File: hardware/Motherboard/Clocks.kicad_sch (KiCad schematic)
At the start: 7 parts, among them U60 74LS04, U61 74LS193, Y1 14MHz

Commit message: WIP
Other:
- moved on the sheet: C1, C2, R20, R21, U60D, U60E, U60F, U61, Y1

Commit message: WIP -rom pack
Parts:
- renumbered C2 to C1, C1 to C2, R20 to R5, R21 to R6, U60 to U31, U61 to U60
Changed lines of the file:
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@@
 		)
 	)
-	(global_label "CLK_3.5MHz"
+	(hierarchical_label "CLK_7MHz"
 		(shape output)
-		(at 223.52 81.28 0)
-		(fields_autoplaced yes)
+		(at 223.52 78.74 0)
 		(effects
 			(font
@@
 			(justify left)
 		)
-		(property "Intersheetrefs" "${INTERSHEET_REFS}"
-			(at 237.8747 81.28 0)
-			(effects
-				(font
-					(size 1.27 1.27)
-				)
-				(justify left)
-				(hide yes)
-			)
-		)
-	)
-	(global_label "CLK_1.75MHz"
+	)
+	(hierarchical_label "CLK_14MHz"
 		(shape output)
-		(at 223.52 83.82 0)
-		(fields_autoplaced yes)
+		(at 223.52 124.46 0)
 		(effects
 			(font
@@
 			(justify left)
 		)
-		(property "Intersheetrefs" "${INTERSHEET_REFS}"
-			(at 239.0842 83.82 0)
-			(effects
-				(font
-					(size 1.27 1.27)
-				)
-				(justify left)
-				(hide yes)
-			)
-		)
-	)
-	(global_label "CLK_7MHz"
+	)
+	(hierarchical_label "CLK_1.75MHz"
 		(shape output)
-		(at 223.52 78.74 0)
-		(fields_autoplaced yes)
+		(at 223.52 83.82 0)
 		(effects
 			(font
@@
 			(justify left)
 		)
-		(property "Intersheetrefs" "${INTERSHEET_REFS}"
-			(at 236.0604 78.74 0)
-			(effects
-				(font
-					(size 1.27 1.27)
-				)
-				(justify left)
-				(hide yes)
-			)
-		)
-	)
-	(global_label "CLK_14MHz"
+	)
+	(hierarchical_label "CLK_3.5MHz"
 		(shape output)
-		(at 223.52 124.46 0)
-		(fields_autoplaced yes)
+		(at 223.52 81.28 0)
 		(effects
 			(font
@@
 			(justify left)
 		)
-		(property "Intersheetrefs" "${INTERSHEET_REFS}"
-			(at 237.2699 124.46 0)
-			(effects
-				(font
-					(size 1.27 1.27)
-				)
-				(justify left)
-				(hide yes)
-			)
-		)
 	)
 	(symbol
@@
 		(dnp no)
 		(fields_autoplaced yes)
-		(property "Reference" "R21"
+		(property "Reference" "R6"
 			(at 104.14 104.14 90)
 			(effects
@@
 		(instances
 			(project "Squale"
-				(path "/9e981419-a202-4dd8-b7ec-e1bde8e7b185/7c4c7ab9-cc93-441e-893a-6812d858b558"
-					(reference "R21")
+				(path "/9e981419-a202-4dd8-b7ec-e1bde8e7b185/70613a33-7fd7-4f8d-95ce-cdec7974bf7d"
+					(reference "R6")
 					(unit 1)
 				)
@@
 		(dnp no)
 		(fields_autoplaced yes)
-		(property "Reference" "R20"
+		(property "Reference" "R5"
 			(at 77.47 104.14 90)
 			(effects
@@
 		)
 		(instances
-			(project ""
-				(path "/9e981419-a202-4dd8-b7ec-e1bde8e7b185/7c4c7ab9-cc93-441e-893a-6812d858b558"
-					(reference "R20")
+			(project "Squale"
+				(path "/9e981419-a202-4dd8-b7ec-e1bde8e7b185/70613a33-7fd7-4f8d-95ce-cdec7974bf7d"
+					(reference "R5")
 					(unit 1)
 				)
@@
 		(dnp no)
 		(fields_autoplaced yes)
-		(property "Reference" "C2"
+		(property "Reference" "C1"
 			(at 91.44 88.9 90)
 			(effects
@@
 		)
 		(instances
-			(project ""
-				(path "/9e981419-a202-4dd8-b7ec-e1bde8e7b185/7c4c7ab9-cc93-441e-893a-6812d858b558"
-					(reference "C2")
+			(project "Squale"
+				(path "/9e981419-a202-4dd8-b7ec-e1bde8e7b185/70613a33-7fd7-4f8d-95ce-cdec7974bf7d"
+					(reference "C1")
 					(unit 1)
 				)
@@
 		(dnp no)
 		(fields_autoplaced yes)
-		(property "Reference" "U60"
+		(property "Reference" "U31"
 			(at 129.54 87.63 0)
 			(effects
@@
 		)
 		(instances
-			(project ""
-				(path "/9e981419-a202-4dd8-b7ec-e1bde8e7b185/7c4c7ab9-cc93-441e-893a-6812d858b558"
-					(reference "U60")
+			(project "Squale"
+				(path "/9e981419-a202-4dd8-b7ec-e1bde8e7b185/70613a33-7fd7-4f8d-95ce-cdec7974bf7d"
+					(reference "U31")
 					(unit 4)
 				)
@@
 		(dnp no)
 		(fields_autoplaced yes)
-		(property "Reference" "U61"
+		(property "Reference" "U60"
 			(at 183.7533 71.12 0)
 			(effects
@@
 		)
 		(instances
-			(project ""
-				(path "/9e981419-a202-4dd8-b7ec-e1bde8e7b185/7c4c7ab9-cc93-441e-893a-6812d858b558"
-					(reference "U61")
+			(project "Squale"
+				(path "/9e981419-a202-4dd8-b7ec-e1bde8e7b185/70613a33-7fd7-4f8d-95ce-cdec7974bf7d"
+					(reference "U60")
 					(unit 1)
 				)
@@
 		(instances
 			(project "Squale"
-				(path "/9e981419-a202-4dd8-b7ec-e1bde8e7b185/7c4c7ab9-cc93-441e-893a-6812d858b558"
+				(path "/9e981419-a202-4dd8-b7ec-e1bde8e7b185/70613a33-7fd7-4f8d-95ce-cdec7974bf7d"
 					(reference "Y1")
 					(unit 1)
@@
 		(dnp no)
 		(fields_autoplaced yes)
-		(property "Reference" "#PWR0171"
+		(property "Reference" "#PWR0168"
 			(at 172.72 91.44 0)
 			(effects
@@
 		(instances
 			(project "Squale"
-				(path "/9e981419-a202-4dd8-b7ec-e1bde8e7b185/7c4c7ab9-cc93-441e-893a-6812d858b558"
-					(reference "#PWR0171")
+				(path "/9e981419-a202-4dd8-b7ec-e1bde8e7b185/70613a33-7fd7-4f8d-95ce-cdec7974bf7d"
+					(reference "#PWR0168")
 					(unit 1)
 				)
@@
 		(dnp no)
 		(fields_autoplaced yes)
-		(property "Reference" "#PWR0170"
+		(property "Reference" "#PWR0169"
 			(at 172.72 99.06 0)
 			(effects
@@
 		(instances
 			(project "Squale"
-				(path "/9e981419-a202-4dd8-b7ec-e1bde8e7b185/7c4c7ab9-cc93-441e-893a-6812d858b558"
-					(reference "#PWR0170")
+				(path "/9e981419-a202-4dd8-b7ec-e1bde8e7b185/70613a33-7fd7-4f8d-95ce-cdec7974bf7d"
+					(reference "#PWR0169")
 					(unit 1)
 				)
@@
 		(dnp no)
 		(fields_autoplaced yes)
-		(property "Reference" "U60"
+		(property "Reference" "U31"
 			(at 105.41 87.63 0)
 			(effects
@@
 		)
 		(instances
-			(project ""
-				(path "/9e981419-a202-4dd8-b7ec-e1bde8e7b185/7c4c7ab9-cc93-441e-893a-6812d858b558"
-					(reference "U60")
+			(project "Squale"
+				(path "/9e981419-a202-4dd8-b7ec-e1bde8e7b185/70613a33-7fd7-4f8d-95ce-cdec7974bf7d"
+					(reference "U31")
 					(unit 5)
 				)
@@
 		(dnp no)
 		(fields_autoplaced yes)
-		(property "Reference" "#PWR0169"
+		(property "Reference" "#PWR0170"
 			(at 181.61 74.93 0)
 			(effects
@@
 		(instances
 			(project "Squale"
-				(path "/9e981419-a202-4dd8-b7ec-e1bde8e7b185/7c4c7ab9-cc93-441e-893a-6812d858b558"
-					(reference "#PWR0169")
+				(path "/9e981419-a202-4dd8-b7ec-e1bde8e7b185/70613a33-7fd7-4f8d-95ce-cdec7974bf7d"
+					(reference "#PWR0170")
 					(unit 1)
 				)
@@
 		(dnp no)
 		(fields_autoplaced yes)
-		(property "Reference" "U60"
+		(property "Reference" "U31"
 			(at 77.47 87.63 0)
 			(effects
@@
 		)
 		(instances
-			(project ""
-				(path "/9e981419-a202-4dd8-b7ec-e1bde8e7b185/7c4c7ab9-cc93-441e-893a-6812d858b558"
-					(reference "U60")
+			(project "Squale"
+				(path "/9e981419-a202-4dd8-b7ec-e1bde8e7b185/70613a33-7fd7-4f8d-95ce-cdec7974bf7d"
+					(reference "U31")
 					(unit 6)
 				)
@@
 		(dnp no)
 		(fields_autoplaced yes)
-		(property "Reference" "U60"
+		(property "Reference" "U31"
 			(at 161.29 148.59 0)
 			(effects
@@
 		)
 		(instances
-			(project ""
-				(path "/9e981419-a202-4dd8-b7ec-e1bde8e7b185/7c4c7ab9-cc93-441e-893a-6812d858b558"
-					(reference "U60")
+			(project "Squale"
+				(path "/9e981419-a202-4dd8-b7ec-e1bde8e7b185/70613a33-7fd7-4f8d-95ce-cdec7974bf7d"
+					(reference "U31")
 					(unit 1)
 				)
@@
 		(dnp no)
 		(fields_autoplaced yes)
-		(property "Reference" "U60"
+		(property "Reference" "U31"
 			(at 161.29 163.83 0)
 			(effects
@@
 		)
 		(instances
-			(project ""
-				(path "/9e981419-a202-4dd8-b7ec-e1bde8e7b185/7c4c7ab9-cc93-441e-893a-6812d858b558"
-					(reference "U60")
+			(project "Squale"
+				(path "/9e981419-a202-4dd8-b7ec-e1bde8e7b185/70613a33-7fd7-4f8d-95ce-cdec7974bf7d"
+					(reference "U31")
 					(unit 2)
 				)
@@
 		(dnp no)
 		(fields_autoplaced yes)
-		(property "Reference" "U60"
+		(property "Reference" "U31"
 			(at 161.29 180.34 0)
 			(effects
@@
 		)
 		(instances
-			(project ""
-				(path "/9e981419-a202-4dd8-b7ec-e1bde8e7b185/7c4c7ab9-cc93-441e-893a-6812d858b558"
-					(reference "U60")
+			(project "Squale"
+				(path "/9e981419-a202-4dd8-b7ec-e1bde8e7b185/70613a33-7fd7-4f8d-95ce-cdec7974bf7d"
+					(reference "U31")
 					(unit 3)
 				)
@@
 		(dnp no)
 		(fields_autoplaced yes)
-		(property "Reference" "C1"
+		(property "Reference" "C2"
 			(at 119.38 87.6299 0)
 			(effects
@@
 		)
 		(instances
-			(project ""
-				(path "/9e981419-a202-4dd8-b7ec-e1bde8e7b185/7c4c7ab9-cc93-441e-893a-6812d858b558"
-					(reference "C1")
+			(project "Squale"
+				(path "/9e981419-a202-4dd8-b7ec-e1bde8e7b185/70613a33-7fd7-4f8d-95ce-cdec7974bf7d"
+					(reference "C2")
 					(unit 1)
 				)
@@
 		(dnp no)
 		(fields_autoplaced yes)
-		(property "Reference" "#PWR0168"
+		(property "Reference" "#PWR0171"
 			(at 181.61 121.92 0)
 			(effects
@@
 		(instances
 			(project "Squale"
-				(path "/9e981419-a202-4dd8-b7ec-e1bde8e7b185/7c4c7ab9-cc93-441e-893a-6812d858b558"
-					(reference "#PWR0168")
+				(path "/9e981419-a202-4dd8-b7ec-e1bde8e7b185/70613a33-7fd7-4f8d-95ce-cdec7974bf7d"
+					(reference "#PWR0171")
 					(unit 1)
 				)

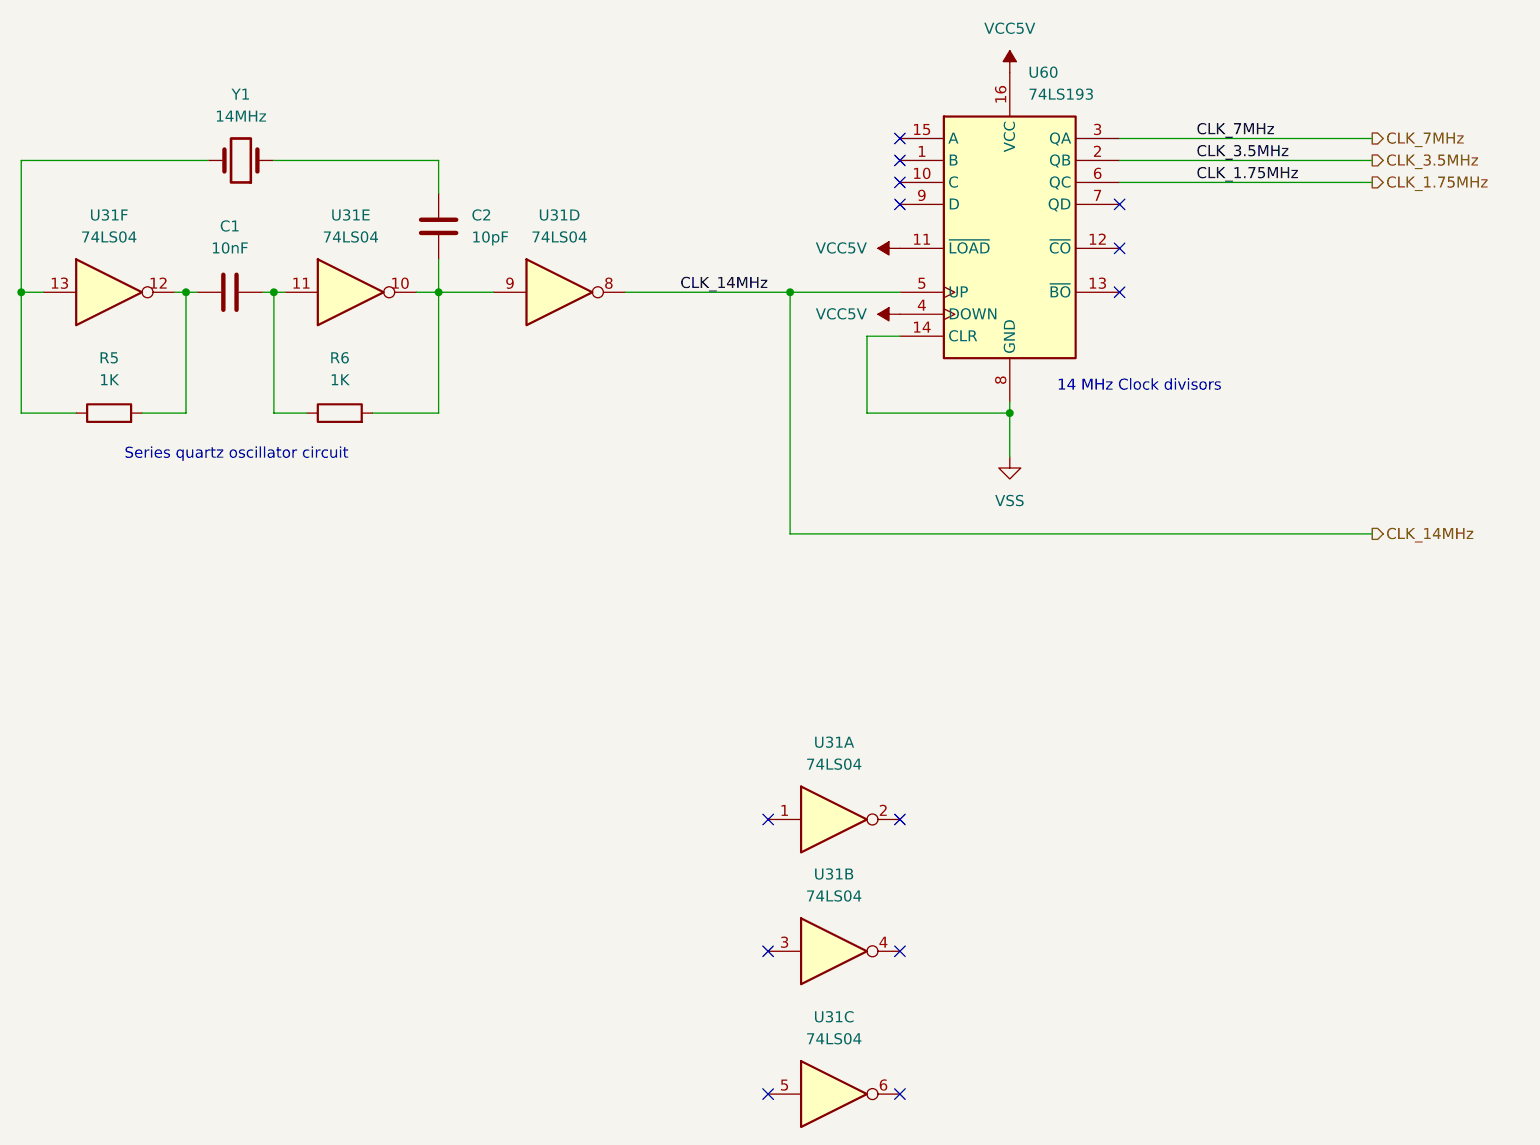
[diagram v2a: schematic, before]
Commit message: S30 bus + annotations fixes.
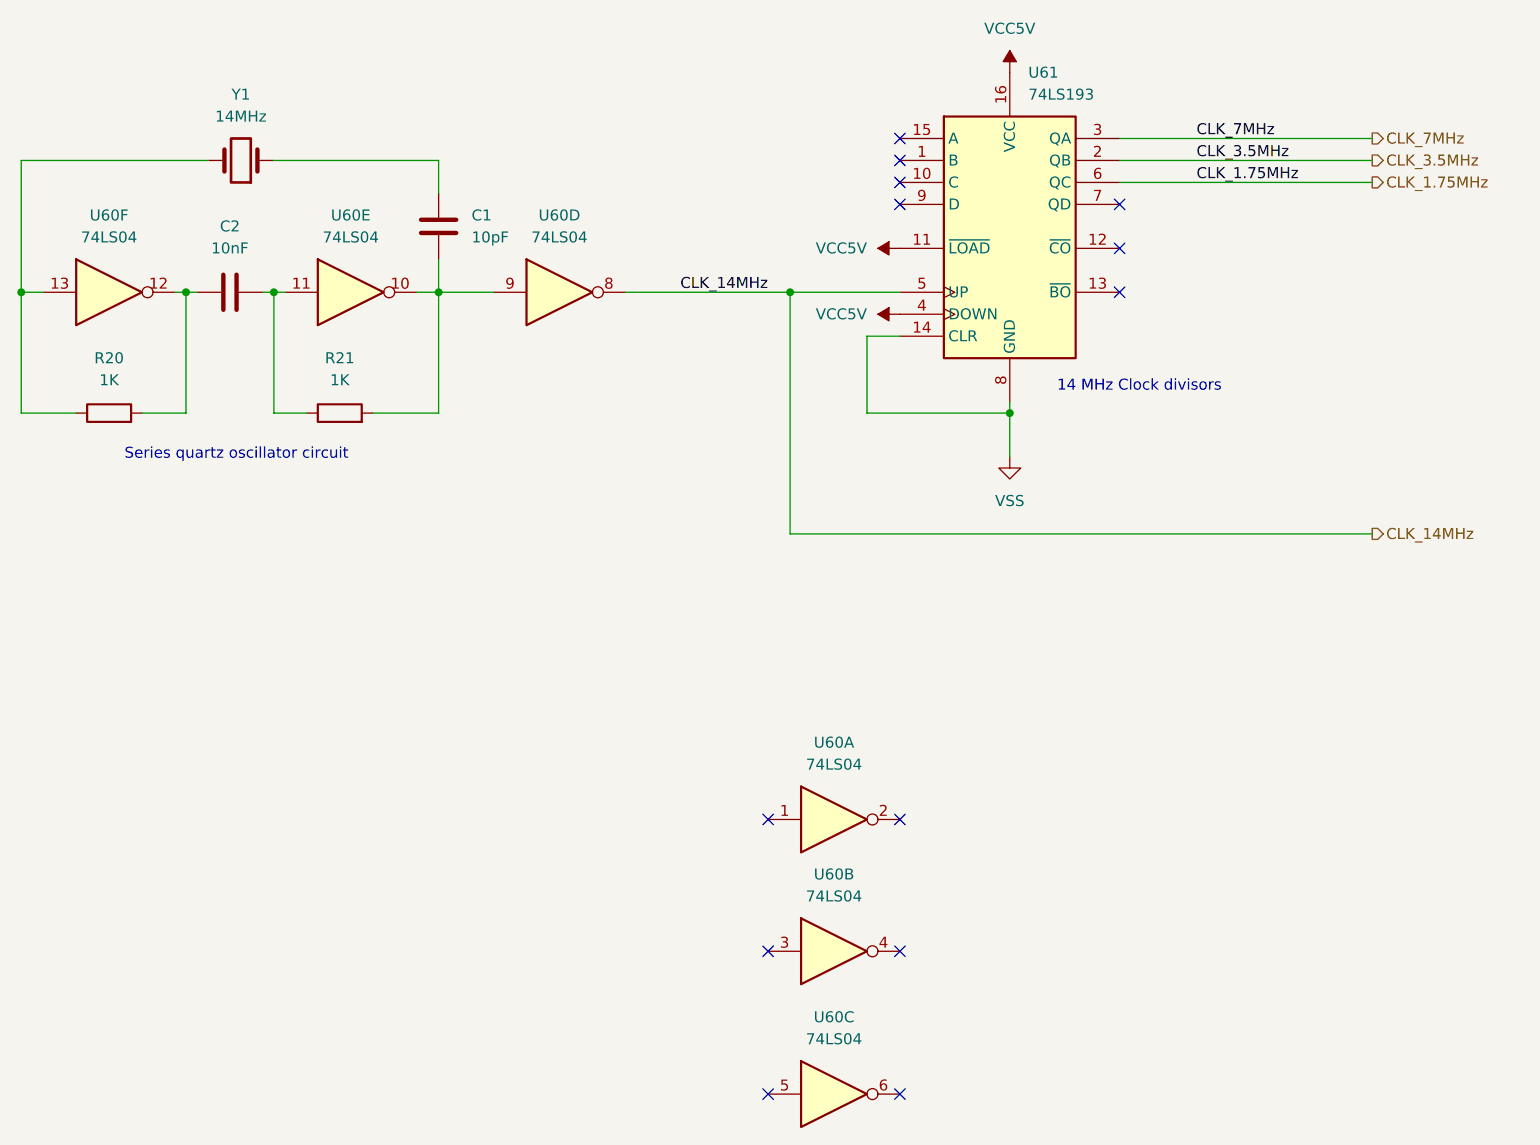
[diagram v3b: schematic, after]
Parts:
- renumbered C2 to C1, C1 to C2, R5 to R20, R6 to R21, U31 to U60, U60 to U61
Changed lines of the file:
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@@
 		(dnp no)
 		(fields_autoplaced yes)
-		(property "Reference" "R6"
+		(property "Reference" "R21"
 			(at 104.14 104.14 90)
 			(effects
@@
 			(project "Squale"
 				(path "/9e981419-a202-4dd8-b7ec-e1bde8e7b185/70613a33-7fd7-4f8d-95ce-cdec7974bf7d"
-					(reference "R6")
+					(reference "R21")
 					(unit 1)
 				)
@@
 		(dnp no)
 		(fields_autoplaced yes)
-		(property "Reference" "R5"
+		(property "Reference" "R20"
 			(at 77.47 104.14 90)
 			(effects
@@
 			(project "Squale"
 				(path "/9e981419-a202-4dd8-b7ec-e1bde8e7b185/70613a33-7fd7-4f8d-95ce-cdec7974bf7d"
-					(reference "R5")
+					(reference "R20")
 					(unit 1)
 				)
@@
 		(dnp no)
 		(fields_autoplaced yes)
-		(property "Reference" "C1"
+		(property "Reference" "C2"
 			(at 91.44 88.9 90)
 			(effects
@@
 			(project "Squale"
 				(path "/9e981419-a202-4dd8-b7ec-e1bde8e7b185/70613a33-7fd7-4f8d-95ce-cdec7974bf7d"
-					(reference "C1")
+					(reference "C2")
 					(unit 1)
 				)
@@
 		(dnp no)
 		(fields_autoplaced yes)
-		(property "Reference" "U31"
+		(property "Reference" "U60"
 			(at 129.54 87.63 0)
 			(effects
@@
 			(project "Squale"
 				(path "/9e981419-a202-4dd8-b7ec-e1bde8e7b185/70613a33-7fd7-4f8d-95ce-cdec7974bf7d"
-					(reference "U31")
+					(reference "U60")
 					(unit 4)
 				)
@@
 		(dnp no)
 		(fields_autoplaced yes)
-		(property "Reference" "U60"
+		(property "Reference" "U61"
 			(at 183.7533 71.12 0)
 			(effects
@@
 			(project "Squale"
 				(path "/9e981419-a202-4dd8-b7ec-e1bde8e7b185/70613a33-7fd7-4f8d-95ce-cdec7974bf7d"
-					(reference "U60")
+					(reference "U61")
 					(unit 1)
 				)
@@
 		(dnp no)
 		(fields_autoplaced yes)
-		(property "Reference" "U31"
+		(property "Reference" "U60"
 			(at 105.41 87.63 0)
 			(effects
@@
 			(project "Squale"
 				(path "/9e981419-a202-4dd8-b7ec-e1bde8e7b185/70613a33-7fd7-4f8d-95ce-cdec7974bf7d"
-					(reference "U31")
+					(reference "U60")
 					(unit 5)
 				)
@@
 		(dnp no)
 		(fields_autoplaced yes)
-		(property "Reference" "U31"
+		(property "Reference" "U60"
 			(at 77.47 87.63 0)
 			(effects
@@
 			(project "Squale"
 				(path "/9e981419-a202-4dd8-b7ec-e1bde8e7b185/70613a33-7fd7-4f8d-95ce-cdec7974bf7d"
-					(reference "U31")
+					(reference "U60")
 					(unit 6)
 				)
@@
 		(dnp no)
 		(fields_autoplaced yes)
-		(property "Reference" "U31"
+		(property "Reference" "U60"
 			(at 161.29 148.59 0)
 			(effects
@@
 			(project "Squale"
 				(path "/9e981419-a202-4dd8-b7ec-e1bde8e7b185/70613a33-7fd7-4f8d-95ce-cdec7974bf7d"
-					(reference "U31")
+					(reference "U60")
 					(unit 1)
 				)
@@
 		(dnp no)
 		(fields_autoplaced yes)
-		(property "Reference" "U31"
+		(property "Reference" "U60"
 			(at 161.29 163.83 0)
 			(effects
@@
 			(project "Squale"
 				(path "/9e981419-a202-4dd8-b7ec-e1bde8e7b185/70613a33-7fd7-4f8d-95ce-cdec7974bf7d"
-					(reference "U31")
+					(reference "U60")
 					(unit 2)
 				)
@@
 		(dnp no)
 		(fields_autoplaced yes)
-		(property "Reference" "U31"
+		(property "Reference" "U60"
 			(at 161.29 180.34 0)
 			(effects
@@
 			(project "Squale"
 				(path "/9e981419-a202-4dd8-b7ec-e1bde8e7b185/70613a33-7fd7-4f8d-95ce-cdec7974bf7d"
-					(reference "U31")
+					(reference "U60")
 					(unit 3)
 				)
@@
 		(dnp no)
 		(fields_autoplaced yes)
-		(property "Reference" "C2"
+		(property "Reference" "C1"
 			(at 119.38 87.6299 0)
 			(effects
@@
 			(project "Squale"
 				(path "/9e981419-a202-4dd8-b7ec-e1bde8e7b185/70613a33-7fd7-4f8d-95ce-cdec7974bf7d"
-					(reference "C2")
+					(reference "C1")
 					(unit 1)
 				)
